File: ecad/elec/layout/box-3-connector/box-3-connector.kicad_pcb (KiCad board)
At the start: 2 copper layers, 72.5 x 7.9 mm, 2 parts

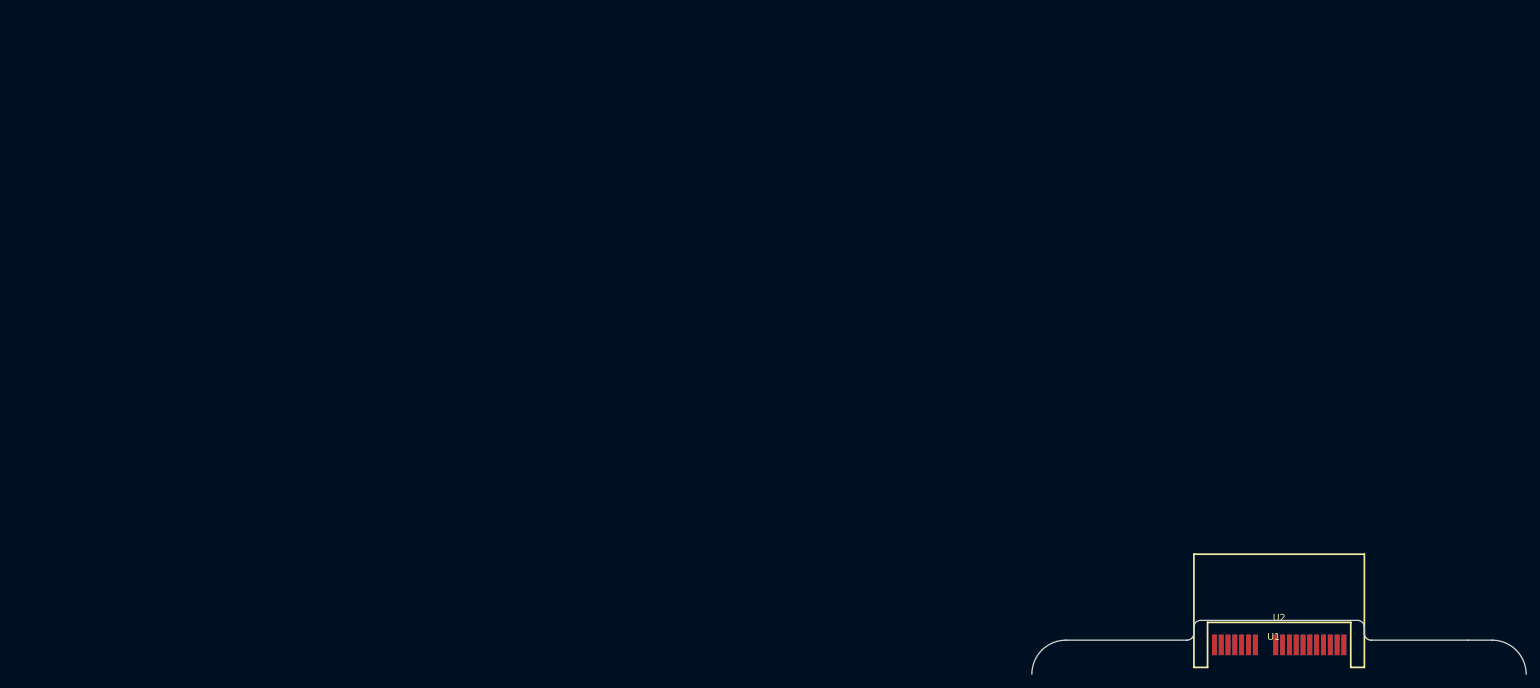
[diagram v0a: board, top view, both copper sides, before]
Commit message: feat(ecad): Update ECAD to support latest atopile and fix some bugs (#119)
* feat(ecad): Update ecad / atopile and improve workflow

* add step file to repo

* add box-3 step file

* improve workflow

* update the action to latest and fix some bugs / spurious issues

* remove legacy files

* update readme

* update deprecations

* improve placement of components and robustness of scripts

* nudge layouts some

* further layout changes

* fixing some issues

* fix broken ci

* minor update

* simple layout

* update to work with latest atopile services (lack thereof)

* update routing

* fix(ecad): vendor atopile registry package for CI builds

packages.atopileapi.com no longer resolves (taken down in the 0.16
platform migration, like the components API), so dependency resolution
of atopile/ti-tps63020@0.4.0 fails in CI and on any machine without a
warm .ato/modules. Commit the installed package (sans .cache) so
`ato build` finds it via its installed-package path and never contacts
the dead registry.

Co-Authored-By: Claude Fable 5 <noreply@anthropic.com>

* fix(ecad): keep vendored package byte-exact (no EOL normalization)

ato validates installed packages against the file hashes in
.package_meta.json; git's CRLF->LF normalization of the STEP files
changed their bytes on checkout, making CI fail with "Package has
local modifications". Exempt ecad/.ato/modules from text normalization
and re-commit the original bytes.

Co-Authored-By: Claude Fable 5 <noreply@anthropic.com>

* fix(ci): disable baked-in ATO_FROZEN and normalize base layout serialization

The atopile-kicad docker image sets ATO_FROZEN=1, silently forcing CI
builds into frozen mode, which fails on phantom in-memory diffs
(locked-attribute defaults, arc direction normalization) that never
reach the file on disk. Pass ATO_FROZEN=0 from the workflow — we verify
layout stability ourselves via canonicalize + git diff.

Also re-serialize box-emu-base.kicad_pcb through the same container
build + canonicalize pip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
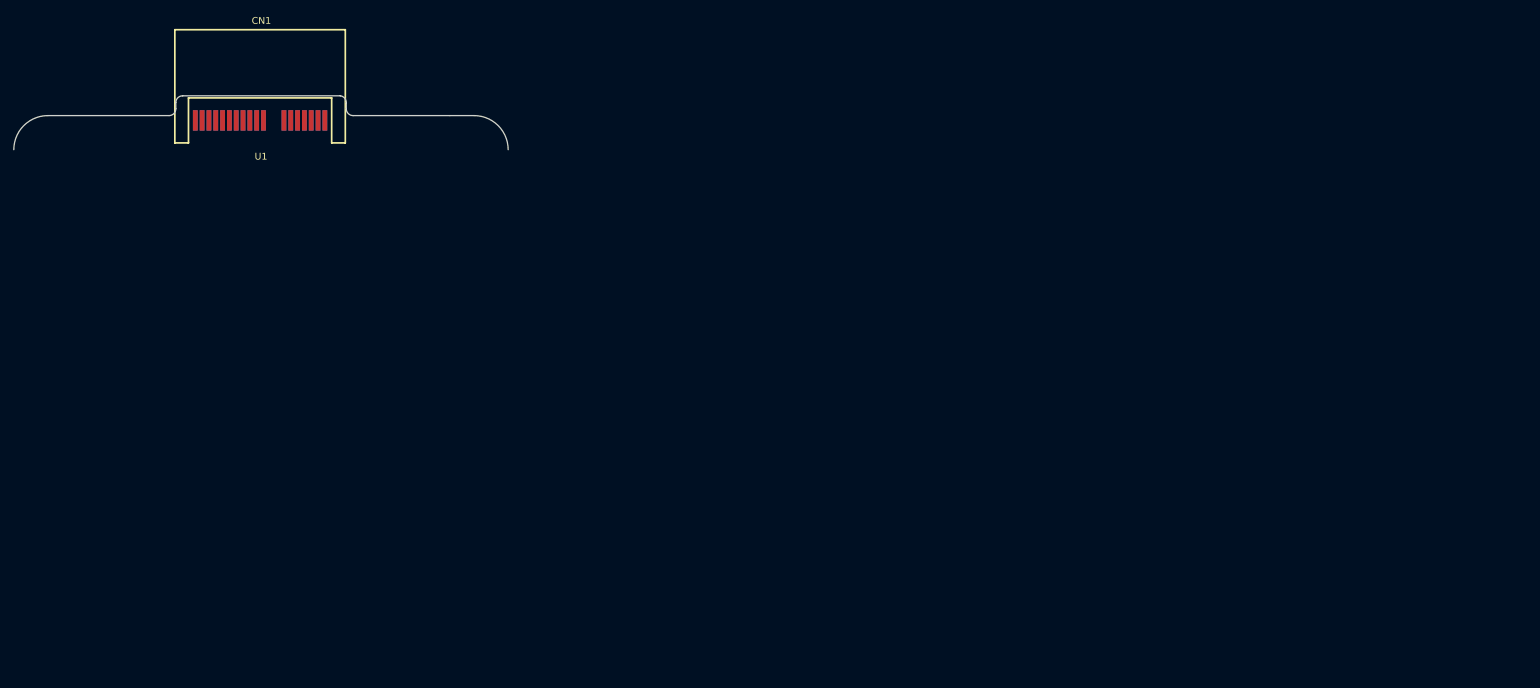
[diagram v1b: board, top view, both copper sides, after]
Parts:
- removed U2: , lib:CONN-SMD_5-1734857-1
- added CN1: , TE_Connectivity_5_1734857_1:CONN-SMD_5-1734857-1, F.Cu at (0.66, 0.71)
- U1: footprint lib:BOX_3_EMU -> BOX_3_EMU_OUTLINE:BOX_3_EMU
- moved U1 168.0 mm to (0.00, 0.00)
